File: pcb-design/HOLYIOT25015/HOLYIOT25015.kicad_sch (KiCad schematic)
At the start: 48 parts, among them J1 VCC, J2 SWDIO, J3 SWDCLK, J4 GND, Q2 SI2301, U1 LIS2DH12, U3 nRF54L15_SOC1, U4 LPS22HB, U5 SHT40-AD1B-R2, Y1 32MHz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

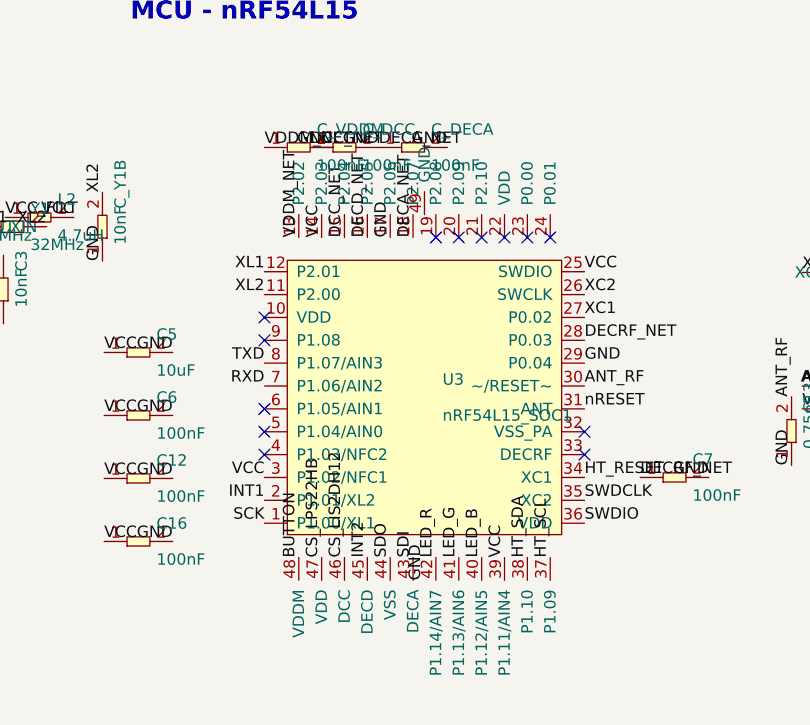
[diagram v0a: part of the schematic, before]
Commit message: Fix GPIO pin assignments on HOLYIOT25015 schematic
Cross-referenced against HOLYIOT-25008 Zephyr board support files
(holyiot_25008_nrf54l15-pinctrl.dtsi / _common.dtsi) for confirmed pins,
and inferred the 25015-only additions (LPS22HB CS, INT_DRDY).

Key corrections:
- P2.02 → SDI (MOSI), was BUTTON
- P2.03 → INT2 (LIS2DH12 IRQ2), was CS_LPS22HB
- P2.04 → SDO (MISO), was CS_LIS2DH12
- P2.05 → CS_LIS2DH12, was INT2
- P2.06 → CS_LPS22HB (inferred), was SDO
- P2.07 → LED_B (Blue), was SDI
- P2.08 → INT_DRDY/LPS22HB (inferred), was LED_R
- P2.09 → LED_R (Red), was LED_G
- P2.10 → NC (unknown), was LED_B
- P1.10 → LED_G (Green), was NC
- P1.13 → BUTTON, was NC

https://claude.ai/code/session_012byMJWHd6Bj8gUwvTH8Mqb
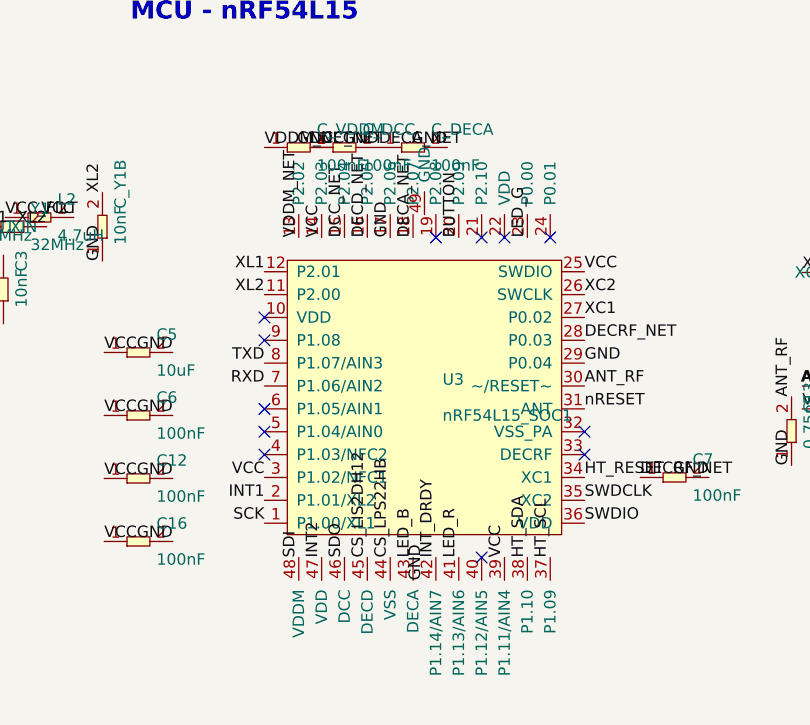
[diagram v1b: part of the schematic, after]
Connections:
- net BUTTON: now also U3.20 (P2.09); no longer U3.48 (VDDM)
- net CS_LIS2DH12: now also U3.45 (DECD); no longer U3.46 (DCC)
- net CS_LPS22HB: now also U3.44 (VSS); no longer U3.47 (VDD)
- net INT2: now also U3.47 (VDD); no longer U3.45 (DECD)
- net INT_DRDY: now also U3.42 (P1.14/AIN7)
- net LED_B: now also U3.43 (DECA); no longer U3.40 (P1.12/AIN5)
- net LED_G: now also U3.23 (P0.00); no longer U3.41 (P1.13/AIN6)
- net LED_R: now also U3.41 (P1.13/AIN6); no longer U3.42 (P1.14/AIN7)
- net SDI: now also U3.48 (VDDM); no longer U3.43 (DECA)
- net SDO: now also U3.46 (DCC); no longer U3.44 (VSS)
- no-connect marks 17 -> 16
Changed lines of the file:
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@@
 		(effects (font (size 1.27 1.27)) (justify right bottom))
 	)
-	(label "BUTTON"
+	(label "SDI"
 		(at 116.0300 172.7800 270)
 		(effects (font (size 1.27 1.27)) (justify left bottom))
 	)
-	(label "CS_LPS22HB"
+	(label "INT2"
 		(at 118.5700 172.7800 270)
 		(effects (font (size 1.27 1.27)) (justify left bottom))
 	)
-	(label "CS_LIS2DH12"
+	(label "SDO"
 		(at 121.1100 172.7800 270)
 		(effects (font (size 1.27 1.27)) (justify left bottom))
 	)
-	(label "INT2"
+	(label "CS_LIS2DH12"
 		(at 123.6500 172.7800 270)
 		(effects (font (size 1.27 1.27)) (justify left bottom))
 	)
-	(label "SDO"
+	(label "CS_LPS22HB"
 		(at 126.1900 172.7800 270)
 		(effects (font (size 1.27 1.27)) (justify left bottom))
 	)
-	(label "SDI"
+	(label "LED_B"
 		(at 128.7300 172.7800 270)
 		(effects (font (size 1.27 1.27)) (justify left bottom))
 	)
-	(label "LED_R"
+	(label "INT_DRDY"
 		(at 131.2700 172.7800 270)
 		(effects (font (size 1.27 1.27)) (justify left bottom))
 	)
-	(label "LED_G"
+	(label "LED_R"
 		(at 133.8100 172.7800 270)
 		(effects (font (size 1.27 1.27)) (justify left bottom))
 	)
-	(label "LED_B"
-		(at 136.3500 172.7800 270)
-		(effects (font (size 1.27 1.27)) (justify left bottom))
-	)
+	(no_connect (at 136.3500 172.7800))
 	(label "VCC"
 		(at 138.8900 172.7800 270)
@@
 	)
 	(no_connect (at 143.9700 137.2200))
-	(no_connect (at 141.4300 137.2200))
+	(label "LED_G"
+		(at 141.4300 137.2200 90)
+		(effects (font (size 1.27 1.27)) (justify left bottom))
+	)
 	(no_connect (at 138.8900 137.2200))
 	(no_connect (at 136.3500 137.2200))
-	(no_connect (at 133.8100 137.2200))
+	(label "BUTTON"
+		(at 133.8100 137.2200 90)
+		(effects (font (size 1.27 1.27)) (justify left bottom))
+	)
 	(no_connect (at 131.2700 137.2200))
 	(label "DECA_NET"
